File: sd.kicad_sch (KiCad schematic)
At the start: 69 parts, among them J2 MicroSD_1140084168, J4 USB-C_GCT_USB4105-GF-A, J5 USB-A_UJ2-AH-4-SMT-TR, U1 USB2642_ML, U2 AP22615A_TSOT26, U3 AP22615A_TSOT26, Y2 Resonator_24MHz_ABM8G

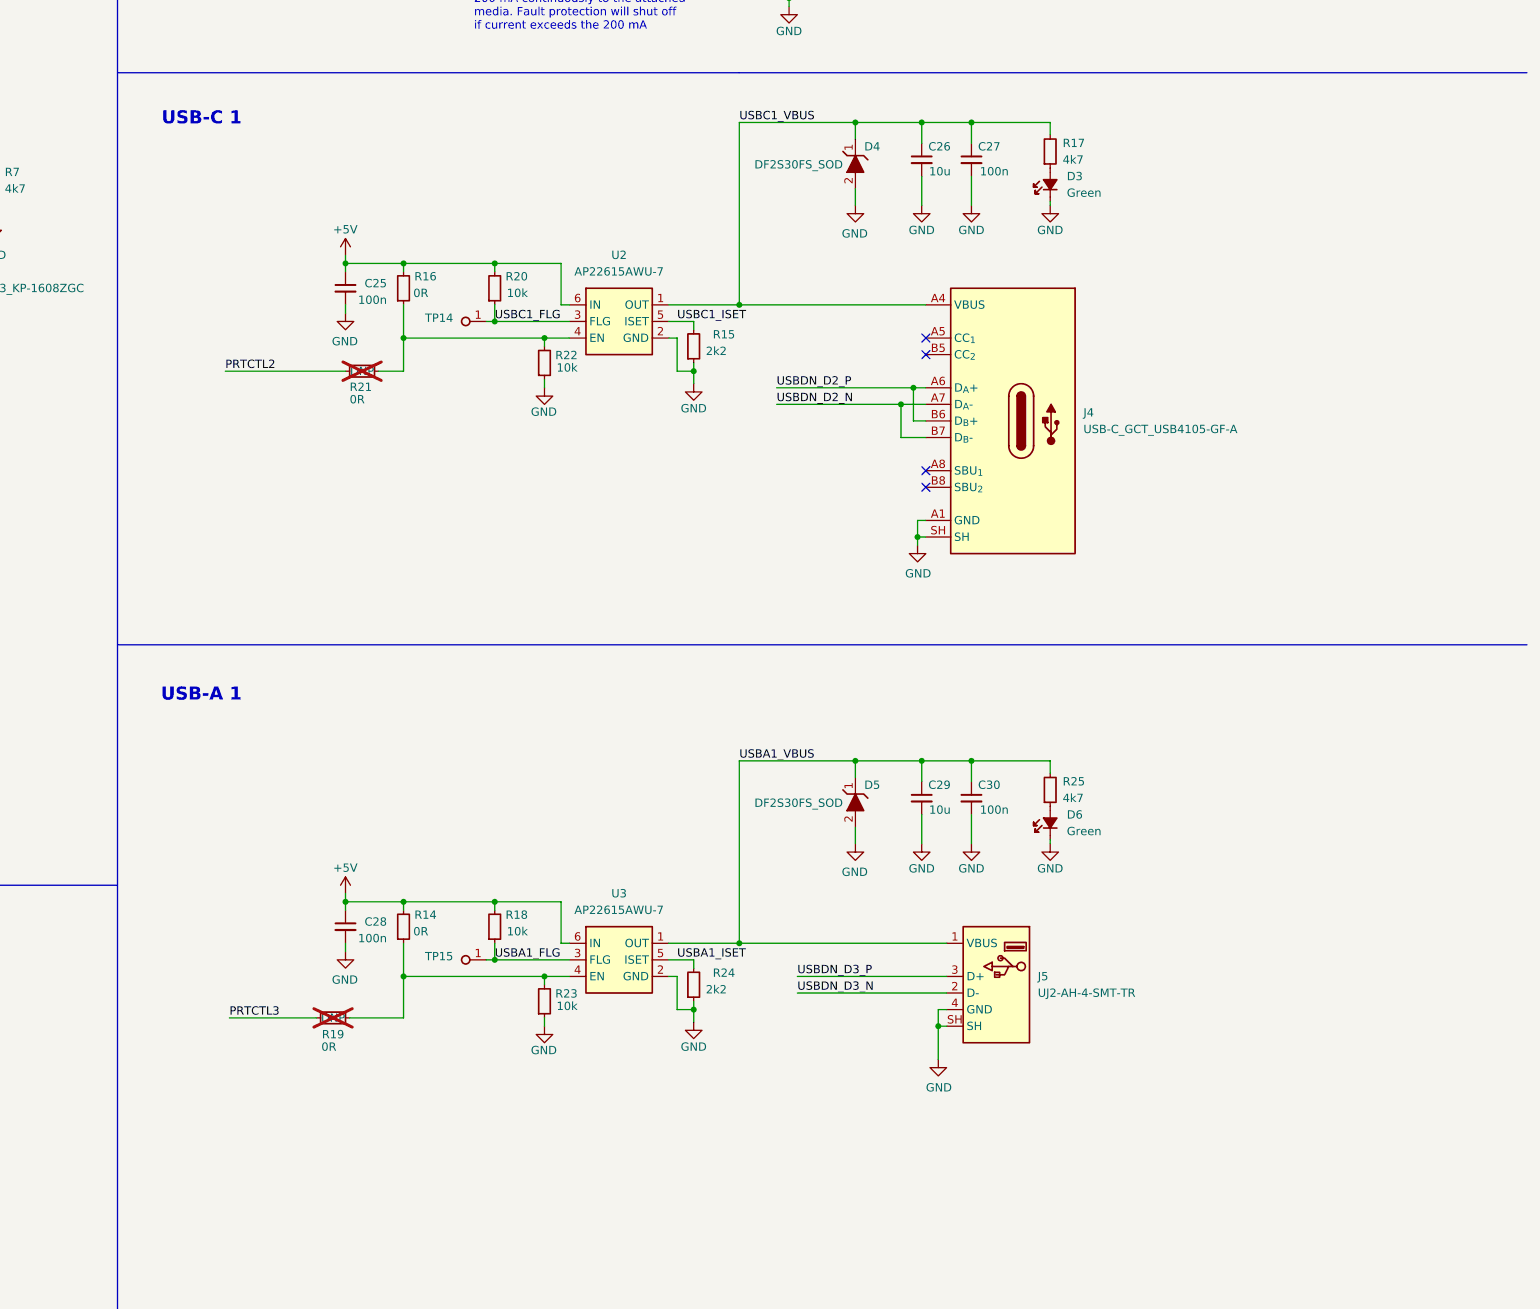
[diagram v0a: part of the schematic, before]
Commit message: [#64333] Added handling for USB-C CC lines and ESD protection according to review
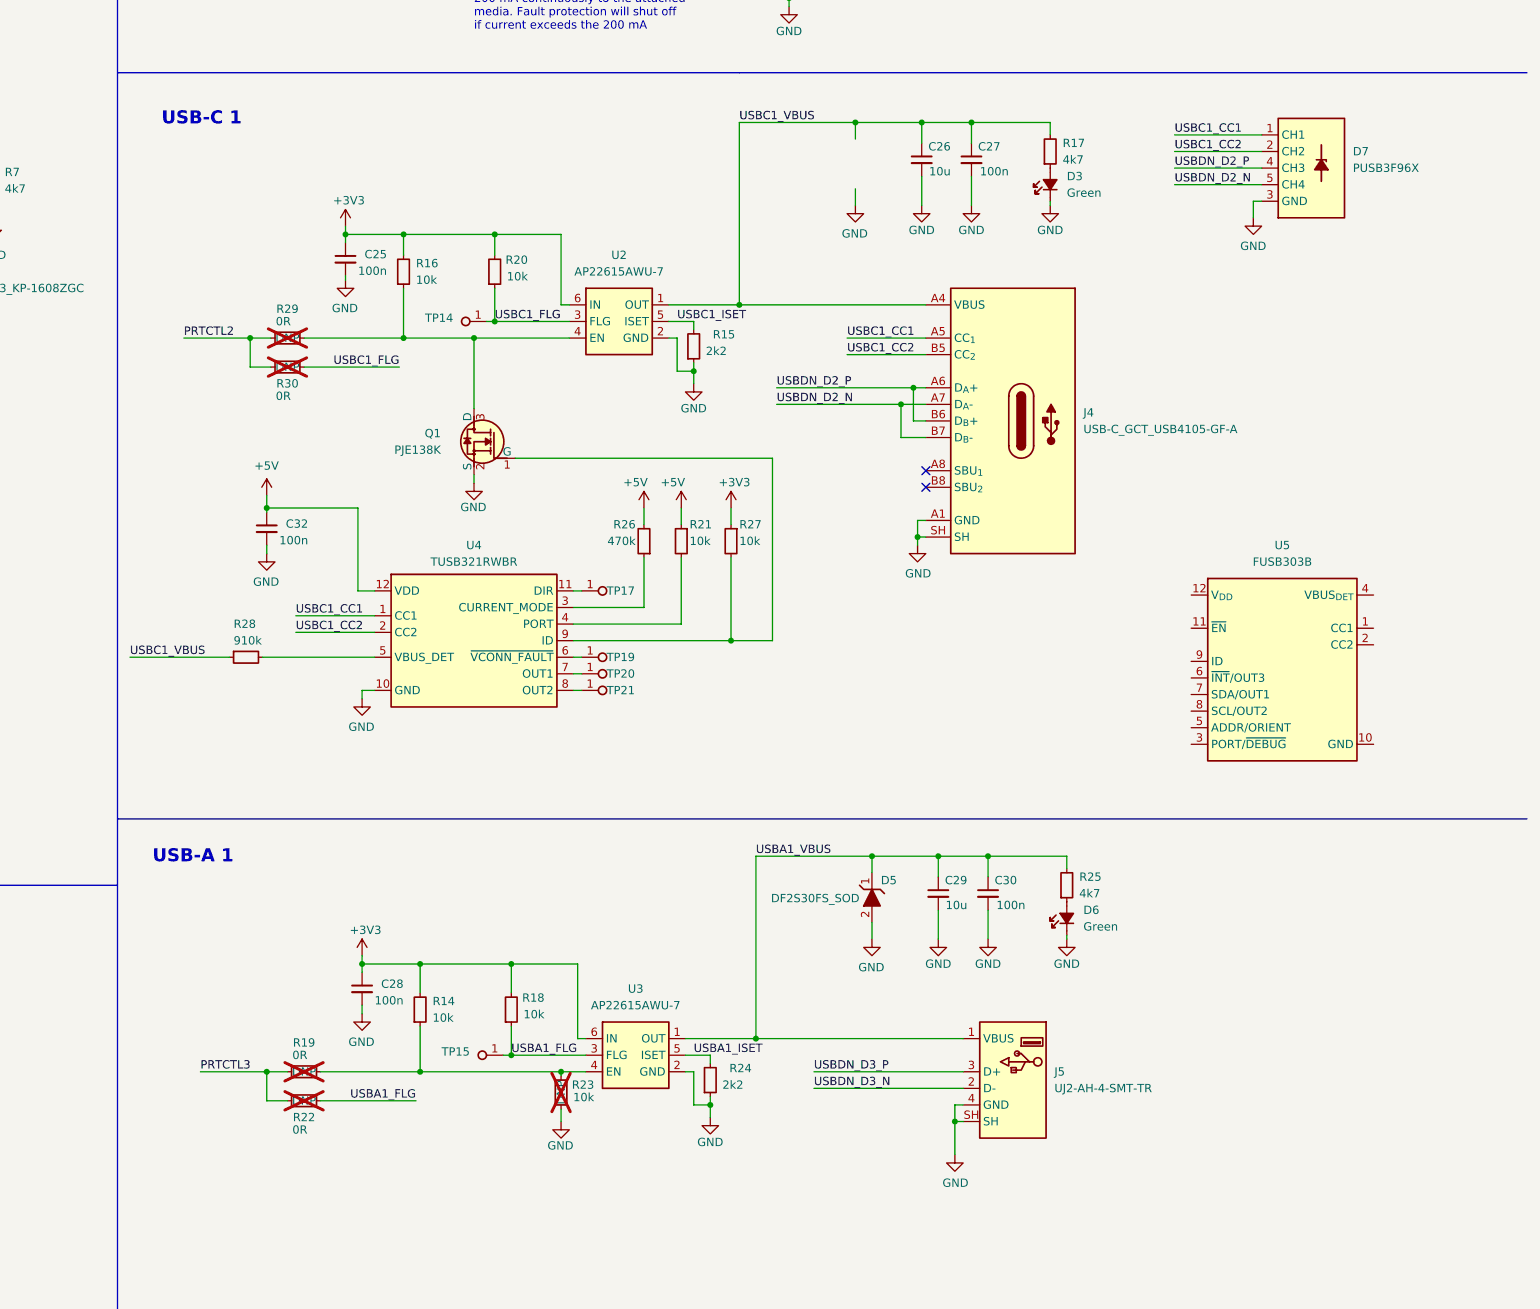
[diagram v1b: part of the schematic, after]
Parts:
- removed D4: DF2S30FS_SOD, antmicro-footprints:SOD-923, symbol antmicroTVSDiodes:DF2S30FS_SOD
- removed R14, R16, R21: R_0R_0402, antmicro-footprints:R_0402_1005Metric, symbol antmicroResistors0402:R_0R_0402
- removed R22: R_10k_0402, antmicro-footprints:R_0402_1005Metric, symbol antmicroResistors0402:R_10k_0402
- added C32: C_100n_0402, antmicro-footprints:C_0402_1005Metric, symbol antmicroCapacitors0402:C_100n_0402
- added D7: PUSB3F96X_PASS, antmicro-footprints:Nexperia_DFN-10_2.5x1mm_P0.5mm, symbol antmicroTVSDiodes:PUSB3F96X_PASS
- added Q1: PJE138K, antmicro-footprints:SOT-523, symbol antmicroTransistorsFETsMOSFETsSingle:PJE138K
- added R14, R16, R21, R27: R_10k_0402, antmicro-footprints:R_0402_1005Metric, symbol antmicroResistors0402:R_10k_0402
- added R22, R29, R30: R_0R_0402, antmicro-footprints:R_0402_1005Metric, symbol antmicroResistors0402:R_0R_0402
- added R26: R_470k_0402, antmicro-footprints:R_0402_1005Metric, symbol antmicroResistors0402:R_470k_0402
- added R28: R_910k_0402, antmicro-footprints:R_0402_1005Metric, symbol antmicroResistors0402:R_910k_0402
- added TP17, TP19, TP20, TP21: TP_0.75mm_SMD, antmicro-footprints:TP_SMD_0.75mm, symbol antmicroTestPoints:TP_0.75mm_SMD
- added U4: TUSB321RWBR, antmicro-footprints:Texas_X2QFN-12_1.6x1.6mm_P0.4mm, symbol antmicroInterfaceControllers:TUSB321RWBR
- added U5: FUSB303B, antmicro-footprints:Texas_X2QFN-12_1.6x1.6mm_P0.4mm, symbol antmicroInterfaceControllers:FUSB303B
- R23: DNP (none) -> DNP; now not fitted; now left out of the parts list
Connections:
- net +3V3: now also C25.1, C28.1, R18.2, R20.2, U2.6 (IN), U3.6 (IN), R14.2, R16.2, R27.1
- net +5V: now also C32.1, R21.1, R26.2, U4.12 (VDD); no longer C25.1, C28.1, R18.2, R20.2, U2.6 (IN), U3.6 (IN)
- net GND: now also C32.2, D7.3 (GND), D7.8 (GND), Q1.2 (S), U4.10 (GND)
- net PRTCTL2: now also R29.1, R30.1
- net PRTCTL3: now also R22.1
- net USBA1_FLG: now also R22.2
- net USBC1_FLG: now also R30.2
- net USBC1_VBUS: now also R28.1
- net USBDN_D2_N: now also D7.5 (CH4), D7.6 (CH4)
- net USBDN_D2_P: now also D7.4 (CH3), D7.7 (CH3)
- net at R19.2, R23.2, U3.4 (EN): now also R14.1
- net at U2.4 (EN): now also Q1.3 (D), R16.1, R29.2
- net USBC1_CC1: now reaches J4.A5 (CC_{1})
- net USBC1_CC1: now also D7.1 (CH1), D7.10 (CH1), U4.1 (CC1)
- net USBC1_CC2: now reaches J4.B5 (CC_{2})
- net USBC1_CC2: now also D7.2 (CH2), D7.9 (CH2), U4.2 (CC2)
- new net: R28.2, U4.5 (VBUS_DET)
- new net: Q1.1 (G), R27.2, U4.9 (ID)
- new net: TP19.1, U4.6 (~{VCONN_FAULT})
- new net: R26.1, U4.3 (CURRENT_MODE)
- new net: TP17.1, U4.11 (DIR)
- new net: TP20.1, U4.7 (OUT1)
- new net: R21.2, U4.4 (PORT)
- new net: TP21.1, U4.8 (OUT2)
- no-connect marks 9 -> 7
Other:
- moved on the sheet: C25, C28, C29, C30, D5, D6, J5, R18, R19, R20, R24, R25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

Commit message: [#64333] Changed USB-C CC controller to FUSB303B
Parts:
- removed C32: C_100n_0402, antmicro-footprints:C_0402_1005Metric, symbol antmicroCapacitors0402:C_100n_0402
- removed D5: DF2S30FS_SOD, antmicro-footprints:SOD-923, symbol antmicroTVSDiodes:DF2S30FS_SOD
- removed R26: R_470k_0402, antmicro-footprints:R_0402_1005Metric, symbol antmicroResistors0402:R_470k_0402
- removed R27: R_10k_0402, antmicro-footprints:R_0402_1005Metric, symbol antmicroResistors0402:R_10k_0402
- removed R28: R_910k_0402, antmicro-footprints:R_0402_1005Metric, symbol antmicroResistors0402:R_910k_0402
- removed R29, R30: R_0R_0402, antmicro-footprints:R_0402_1005Metric, symbol antmicroResistors0402:R_0R_0402
- removed TP19, TP20, TP21: TP_0.75mm_SMD, antmicro-footprints:TP_SMD_0.75mm, symbol antmicroTestPoints:TP_0.75mm_SMD
- removed U4: TUSB321RWBR, antmicro-footprints:Texas_X2QFN-12_1.6x1.6mm_P0.4mm, symbol antmicroInterfaceControllers:TUSB321RWBR
- added C33: C_100n_0402, antmicro-footprints:C_0402_1005Metric, symbol antmicroCapacitors0402:C_100n_0402
- added D4, D5: PESD5Z5_0F, antmicro-footprints:SOD-523, symbol antmicroTVSDiodes:PESD5Z5_0F
- added D8: PUSB3F96X_PASS, antmicro-footprints:Nexperia_DFN-10_2.5x1mm_P0.5mm, symbol antmicroTVSDiodes:PUSB3F96X_PASS
- added Q2: PJE138K, antmicro-footprints:SOT-523, symbol antmicroTransistorsFETsMOSFETsSingle:PJE138K
- added R31, R32, R33, R34: R_10k_0402, antmicro-footprints:R_0402_1005Metric, symbol antmicroResistors0402:R_10k_0402
- added TP18: TP_0.75mm_SMD, antmicro-footprints:TP_SMD_0.75mm, symbol antmicroTestPoints:TP_0.75mm_SMD
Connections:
- net +5V: now also U5.12 (V_{DD}), C33.1, R31.2, R33.2, R34.2; no longer R21.1
- net GND: now also R21.1, U5.10 (GND), U5.7 (SDA/OUT1), C33.2, D4.2 (A), D5.2 (A), D8.3 (GND), D8.8 (GND), Q2.2 (S), R32.1
- net PRTCTL2: now also Q2.1 (G), R32.2
- net USBA1_VBUS: now also D5.1 (C)
- net USBC1_CC1: now also U5.2 (CC2)
- net USBC1_CC2: now also U5.1 (CC1)
- net USBC1_VBUS: now also U5.4 (VBUS_{DET}), D4.1 (C)
- net USBDN_D3_N: now also D8.2 (CH2), D8.9 (CH2)
- net USBDN_D3_P: now also D8.1 (CH1), D8.10 (CH1)
- net ID: now reaches Q1.1 (G)
- net ID: now also R21.2, U5.9 (ID)
- net at U5.11 (~{EN}): now also Q2.3 (D), R31.1
- net at U5.3 (PORT/~{DEBUG}): now also R34.1
- net at U5.5 (ADDR/ORIENT): now also TP17.1
- net at U5.6 (~{INT}/OUT3): now also TP18.1
- net at U5.8 (SCL/OUT2): now also R33.1
- new net: D8.4 (CH3), D8.7 (CH3)
- new net: D8.5 (CH4), D8.6 (CH4)
- no-connect marks 7 -> 9
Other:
- note added: "ESD/EMI protection"
- note added: "USB-C 1 CC controller"
- moved on the sheet: C21, C22, C23, C24, C26, C27, C28, C29, C30, D3, D6, D7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
